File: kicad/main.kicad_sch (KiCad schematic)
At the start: 41 parts, among them J1 Jack-DC, J2 LCD, J3 Addr, J4 IO~{EN}_{[2..7]}, J5 Data, J6 Control, J7 VIA_A, J8 VIA_B, SW1 Step, SW2 Reset, X1 1 MHz

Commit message: Add Traco Power TSR 1-2450
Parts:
- REG1: footprint Package_TO_SOT_THT:TO-220-3_Vertical -> kicad:CONV_TSR_1-2450
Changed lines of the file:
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@@
     (property "Reference" "REG1" (id 0) (at 46.99 109.22 0))
     (property "Value" "TSC 1-2450" (id 1) (at 46.99 111.76 0))
-    (property "Footprint" "Package_TO_SOT_THT:TO-220-3_Vertical" (id 2) (at 46.99 112.395 0)
+    (property "Footprint" "kicad:CONV_TSR_1-2450" (id 2) (at 46.99 112.395 0)
       (effects (font (size 1.27 1.27) italic) hide)
     )
@@
     )
     (path "/997a0ae6-d56b-48b6-8b5e-763a9bca4e41"
-      (reference "REG1") (unit 1) (value "TSC 1-2450") (footprint "Package_TO_SOT_THT:TO-220-3_Vertical")
+      (reference "REG1") (unit 1) (value "TSC 1-2450") (footprint "kicad:CONV_TSR_1-2450")
     )
     (path "/0fe13bfc-8702-4c87-b179-d843f7a65b2c"

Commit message: Update ROM code to be runnable in sim65, increase PCB spacing at borders
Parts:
- RES1, STEP1: footprint Package_TO_SOT_THT:TO-92_Inline -> Package_TO_SOT_THT:TO-92_Inline_Wide
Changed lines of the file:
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@@
       (effects (font (size 1.27 1.27)) (justify right))
     )
-    (property "Footprint" "Package_TO_SOT_THT:TO-92_Inline" (id 2) (at 120.65 100.33 0)
+    (property "Footprint" "Package_TO_SOT_THT:TO-92_Inline_Wide" (id 2) (at 120.65 100.33 0)
       (effects (font (size 1.27 1.27)) hide)
     )
@@
       (effects (font (size 1.27 1.27)) (justify right))
     )
-    (property "Footprint" "Package_TO_SOT_THT:TO-92_Inline" (id 2) (at 95.25 100.33 0)
+    (property "Footprint" "Package_TO_SOT_THT:TO-92_Inline_Wide" (id 2) (at 95.25 100.33 0)
       (effects (font (size 1.27 1.27)) hide)
     )
@@
     )
     (path "/0fe13bfc-8702-4c87-b179-d843f7a65b2c"
-      (reference "RES1") (unit 1) (value "DS1813") (footprint "Package_TO_SOT_THT:TO-92_Inline")
+      (reference "RES1") (unit 1) (value "DS1813") (footprint "Package_TO_SOT_THT:TO-92_Inline_Wide")
     )
     (path "/568d8db0-0878-4f6c-a240-e9c0b9b07dff"
@@
     )
     (path "/5f1426dc-69bd-4410-9694-fac63644cb08"
-      (reference "STEP1") (unit 1) (value "DS1813") (footprint "Package_TO_SOT_THT:TO-92_Inline")
+      (reference "STEP1") (unit 1) (value "DS1813") (footprint "Package_TO_SOT_THT:TO-92_Inline_Wide")
     )
     (path "/cdb98851-649e-4ab7-9299-efd45c6ad697"

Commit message: V11
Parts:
- added C6: 0.1uF, Capacitor_THT:C_Disc_D3.0mm_W2.0mm_P2.50mm, symbol Device:C
- added C8, C9: 20nF, Capacitor_THT:C_Disc_D3.0mm_W2.0mm_P2.50mm, symbol Device:C
- added unit 4 of IO2
- added unit 5 of IO2
- added unit 3 of IO2
- added unit 1 of IO2
- added unit 4 of RW1
- added U1: 8580, Package_DIP:DIP-28_W15.24mm, symbol 65xx:8580
- renumbered C2 to C1, C8 to C10, C7 to C11, C9 to C12, C1 to C2, C6 to C3, C3 to C5, C5 to C7, RW1 to IO2, J7 to J5, J8 to J6, J5 to J7, J6 to J8
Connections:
- net +5V: now also C10.2, C6.1, IO2.14 (VCC); no longer C10.1
- net A_{0}: now also U1.9 (A0)
- net A_{1}: now also U1.10 (A1)
- net A_{2}: now also U1.11 (A2)
- net A_{3}: now also U1.12 (A3)
- net A_{4}: now also U1.13 (A4)
- net D_{0}: now also U1.15 (D0)
- net D_{1}: now also U1.16 (D1)
- net D_{2}: now also U1.17 (D2)
- net D_{3}: now also U1.18 (D3)
- net D_{4}: now also U1.19 (D4)
- net D_{5}: now also U1.20 (D5)
- net D_{6}: now also U1.21 (D6)
- net D_{7}: now also U1.22 (D7)
- net GND: now also C10.1, C6.2, IO2.7 (GND), U1.14 (GND); no longer C10.2
- net R~{W}: now also J2.5 (Pin_5), RW1.10, U1.7 (R/~{W}); no longer RW1.9
- net ~{RES}: now also U1.5 (~{RES})
- net ~{WD}: no longer J2.5 (Pin_5)
- net Ф2: now also CPU1.37 (ϕ0), IO2.5, JP1.2 (C), RW1.9, U1.6 (ϕ2); no longer CPU1.39 (ϕ2), RW1.10
- net LCD~{EN}: no longer names the net of IO1.15 (O0)
- net LCD~{EN}: now also IO2.1, IO2.2; no longer J2.6 (Pin_6)
- new net: C9.1, U1.3 (CAP2A)
- new net: C9.2, U1.4 (CAP2B)
- new net: IO2.3, IO2.4
- new net: IO2.10, IO2.6, IO2.9
- new net: C8.1, U1.1 (CAP1A)
- new net: C8.2, U1.2 (CAP1B)
- new net LCD/EN: IO2.8, J2.6 (Pin_6)
- no-connect marks 11 -> 23
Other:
- note added: "$D400-$D4FF reserved for SID"
- note added: "(PHI1O)"
- note added: "(PHI2)"
- note added: "(PHI2O)"
- note added: "1"
- note added: "2"
- note added: "8 256-byte IO blocks (C000-C7FF)"
- note added: "Memory"
- note added: "Notes:"
- note added: "The Heart"
- note added: "The Mind"
- note added: "The Soul (TBD)"
- note added: "[1] Compatible with: 1008, 2008, & 4008 [2] I initially set this to ~{WD}, but later changed it to R~{W}"
- note removed: "$D400-$CDFF reserved for SID"
- note removed: "8 256-byte I/O segments from C000 to C7FF"
- note removed: "Clock & Reset"
- note removed: "Compatible with 1008, 2008, & 4008"
- title: 6502 SBC -> 65ad02
- moved on the sheet: ADDR1A, ADDR1B, ADDR1C, ADDR1E, C1, C10, C11, C12, C2, C3, C4, C5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

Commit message: V0.12: (PS/2 & 4-bit LCD with VIA), cleanup kicad libs
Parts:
- removed C6: 0.1uF, Capacitor_THT:C_Disc_D3.0mm_W2.0mm_P2.50mm, symbol Device:C
- removed C8, C9: 20nF, Capacitor_THT:C_Disc_D3.0mm_W2.0mm_P2.50mm, symbol Device:C
- removed IO2: 74HC00, Package_DIP:DIP-14_W7.62mm, symbol 74xx:74HC00
- removed J3: Addr, Connector_PinHeader_2.54mm:PinHeader_1x08_P2.54mm_Vertical, symbol Connector:Conn_01x08_Male
- removed J5: VIA_A, Connector_PinHeader_2.54mm:PinHeader_2x07_P2.54mm_Vertical, symbol Connector:Conn_01x14_Male
- removed J6: VIA_B, Connector_PinHeader_2.54mm:PinHeader_2x07_P2.54mm_Vertical, symbol Connector:Conn_01x14_Male
- removed J7: Data, Connector_PinHeader_2.54mm:PinHeader_1x08_P2.54mm_Vertical, symbol Connector:Conn_01x08_Male
- removed J8: Control, Connector_PinHeader_2.54mm:PinHeader_2x05_P2.54mm_Vertical, symbol Connector:Conn_01x10_Male
- removed U1: 8580, Package_DIP:DIP-28_W15.24mm, symbol 65xx:8580
- added J3: Bus, Connector_PinHeader_2.54mm:PinHeader_2x08_P2.54mm_Vertical, symbol Connector:Conn_01x16_Male
- added J4: VIA_B, Connector_PinHeader_2.54mm:PinHeader_2x06_P2.54mm_Vertical, symbol Connector:Conn_01x12_Male
- added J6: Control, Connector_PinHeader_2.54mm:PinHeader_2x04_P2.54mm_Vertical, symbol Connector:Conn_01x08_Male
- added P1: Mini-DIN-6, Custom_Footprints:Connector_Mini-DIN_Female_6Pin_2rows, symbol Custom_Symbols_Library:Mini-DIN_6pins_ver3
- added R8, R9: 1K, Resistor_THT:R_Axial_DIN0204_L3.6mm_D1.6mm_P7.62mm_Horizontal, symbol Device:R
- X1: value 1 MHz -> 4 MHz; footprint Oscillator:Oscillator_DIP-14 -> Package_DIP:DIP-14_W7.62mm_Socket
- renumbered C4 to C3, C5 to C4, C3 to C5, C7 to C6, C11 to C7, C10 to C8, C12 to C9, J4 to J5
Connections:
- net LCD/EN is gone; now on net PA_{4}: J2.6 (Pin_6)
- net +5V: now also J4.2 (Pin_2), J6.2 (Pin_2), P1.4, R8.2, R9.2
- net A_{0}: now also J3.1 (Pin_1); no longer J2.4 (Pin_4)
- net A_{1}: now also J3.2 (Pin_2)
- net A_{2}: now also J3.3 (Pin_3)
- net A_{3}: now also J3.4 (Pin_4)
- net A_{4}: now also J3.5 (Pin_5)
- net A_{5}: now also J3.6 (Pin_6)
- net A_{6}: now also J3.7 (Pin_7)
- net A_{7}: now also J3.8 (Pin_8)
- net D_{0}: now also J3.9 (Pin_9); no longer J2.7 (Pin_7)
- net D_{1}: now also J3.10 (Pin_10); no longer J2.8 (Pin_8)
- net D_{2}: now also J3.11 (Pin_11); no longer J2.9 (Pin_9)
- net D_{3}: now also J3.12 (Pin_12); no longer J2.10 (Pin_10)
- net D_{4}: now also J3.13 (Pin_13); no longer J2.11 (Pin_11)
- net D_{5}: now also J3.14 (Pin_14); no longer J2.12 (Pin_12)
- net D_{6}: now also J3.15 (Pin_15); no longer J2.13 (Pin_13)
- net D_{7}: now also J3.16 (Pin_16); no longer J2.14 (Pin_14)
- net GND: now also J4.1 (Pin_1), J6.1 (Pin_1), P1.3
- net R~{W}: now also J6.3 (Pin_3); no longer J2.5 (Pin_5)
- net VIA~{EN}: now also IO1.15 (O0); no longer IO1.14 (O1)
- net ~{IRQ}: now also J6.7 (Pin_7)
- net ~{RD}: now also J6.4 (Pin_4)
- net ~{RES}: now also J6.8 (Pin_8)
- net ~{WD}: now also J6.5 (Pin_5)
- net Ф2: now also J6.6 (Pin_6)
- net at VIA1.17 (PB7): now also J4.10 (Pin_10)
- net at VIA1.18 (CB1): now also J4.11 (Pin_11)
- net at VIA1.19 (CB2): now also J4.12 (Pin_12)
- net at VIA1.10 (PB0): now also J4.3 (Pin_3)
- net at VIA1.11 (PB1): now also J4.4 (Pin_4)
- net at VIA1.12 (PB2): now also J4.5 (Pin_5)
- net at VIA1.13 (PB3): now also J4.6 (Pin_6)
- net at VIA1.14 (PB4): now also J4.7 (Pin_7)
- net at VIA1.15 (PB5): now also J4.8 (Pin_8)
- net at VIA1.16 (PB6): now also J4.9 (Pin_9)
- net PA_{7}: now reaches VIA1.9 (PA7)
- net PA_{7}: now also P1.1, R9.1
- net CA1: now reaches VIA1.40 (CA1)
- net CA1: now also P1.5, R8.1
- net PA_{0}: now reaches VIA1.2 (PA0)
- net PA_{0}: now also J2.11 (Pin_11)
- net PA_{1}: now reaches VIA1.3 (PA1)
- net PA_{1}: now also J2.12 (Pin_12)
- net PA_{2}: now reaches VIA1.4 (PA2)
- net PA_{2}: now also J2.13 (Pin_13)
- net PA_{3}: now reaches VIA1.5 (PA3)
- net PA_{3}: now also J2.14 (Pin_14)
- net PA_{4}: now reaches VIA1.6 (PA4)
- net PA_{5}: now reaches VIA1.7 (PA5)
- net PA_{5}: now also J2.5 (Pin_5)
- net PA_{6}: now reaches VIA1.8 (PA6)
- net PA_{6}: now also J2.4 (Pin_4)
- no-connect marks 23 -> 22
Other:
- note added: "PS/2 Keyboard Connector"
- note added: "[1] Compatible with: 1008, 2008, & 4008"
- note removed: "$D100-$D1FF"
- note removed: "2"
- note removed: "The Soul (TBD)"
- note removed: "[1] Compatible with: 1008, 2008, & 4008 [2] I initially set this to ~{WD}, but later changed it to R~{W}"
- moved on the sheet: ADDR1A, ADDR1B, ADDR1C, ADDR1D, ADDR1E, C3, C5, C7, IO1, J5, RV1, RW1A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

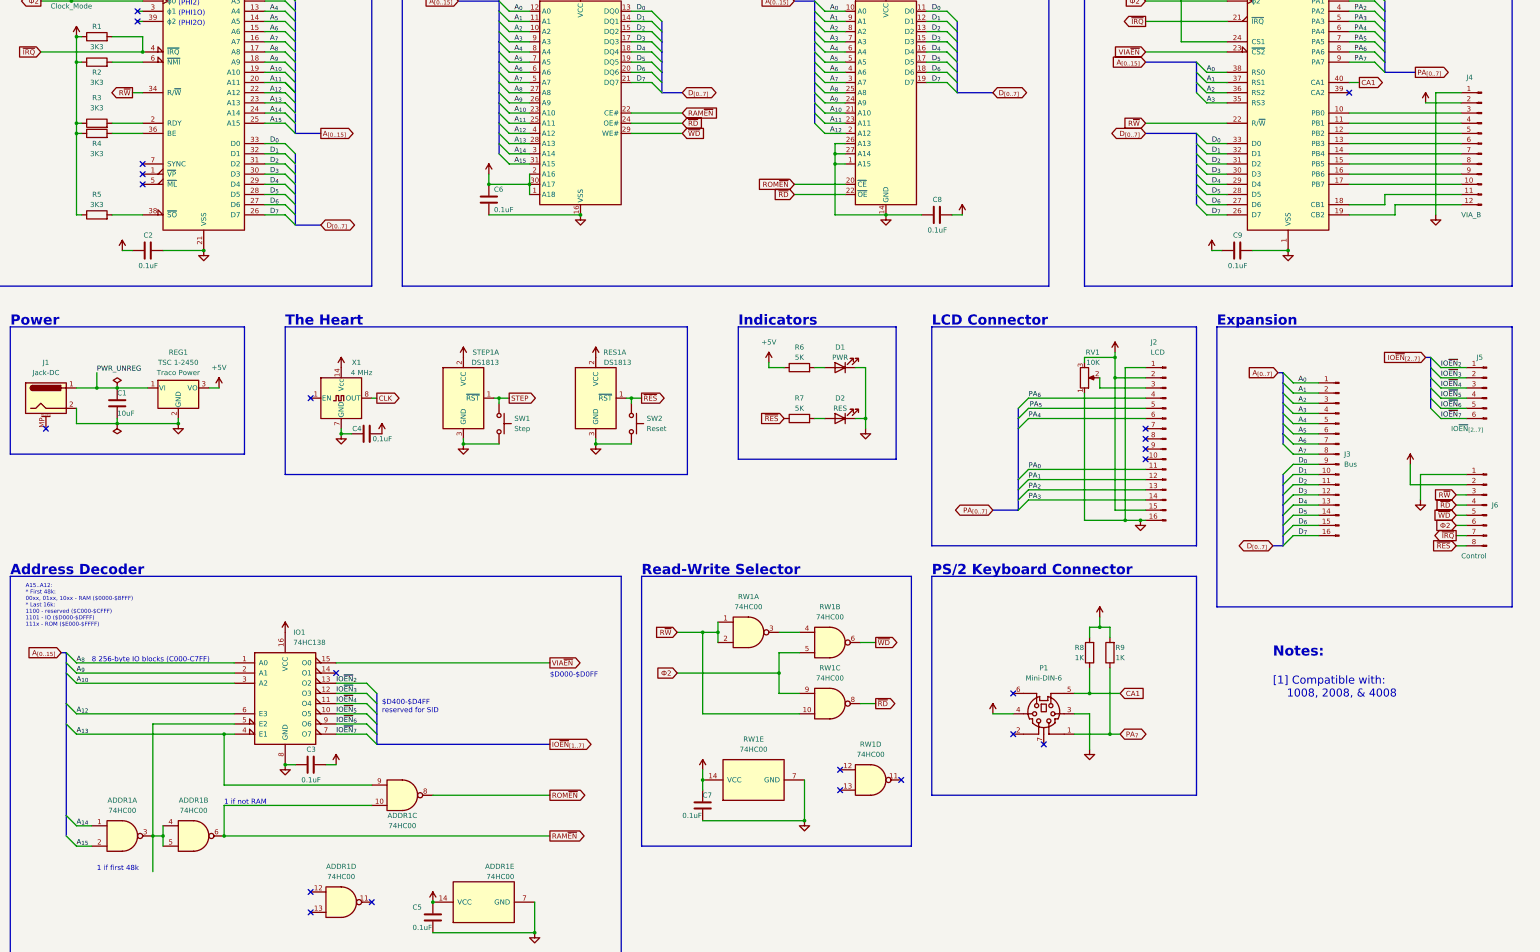
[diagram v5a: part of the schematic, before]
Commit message: Test illegal opcodes, update SPI pin assignments, update V12 PCB
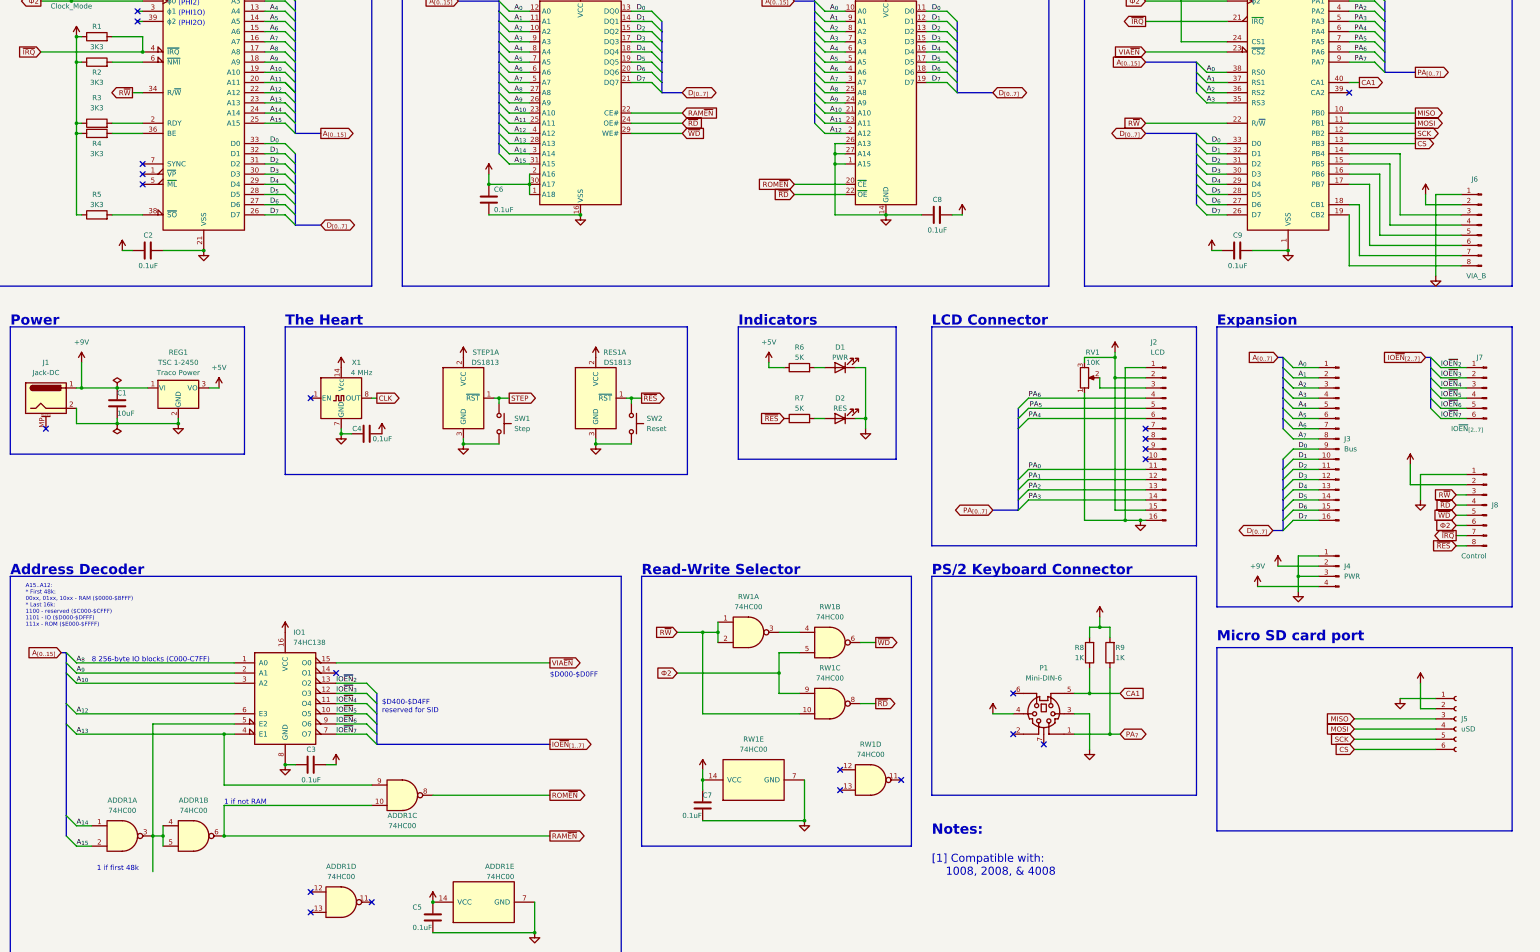
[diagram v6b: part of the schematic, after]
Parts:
- removed J4: VIA_B, Connector_PinHeader_2.54mm:PinHeader_2x06_P2.54mm_Vertical, symbol Connector:Conn_01x12_Male
- added J4: PWR, Connector_PinHeader_2.54mm:PinHeader_2x02_P2.54mm_Vertical, symbol Connector:Conn_01x04_Male
- added J5: uSD, Connector_PinSocket_2.54mm:PinSocket_1x06_P2.54mm_Vertical, symbol Connector:Conn_01x06_Female
- added J6: VIA_B, Connector_PinHeader_2.54mm:PinHeader_2x04_P2.54mm_Vertical, symbol Connector:Conn_01x08_Male
- R1, R2, R3, R4, R5, R8, R9: footprint Resistor_THT:R_Axial_DIN0204_L3.6mm_D1.6mm_P7.62mm_Horizontal -> Resistor_THT:R_Axial_DIN0204_L3.6mm_D1.6mm_P2.54mm_Vertical
- renumbered J5 to J7, J6 to J8
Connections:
- net +5V: now also J4.2 (Pin_2), J5.2 (Pin_2), J6.2 (Pin_2)
- net GND: now also J4.1 (Pin_1), J4.3 (Pin_3), J5.1 (Pin_1), J6.1 (Pin_1)
- net MISO: now reaches VIA1.10 (PB0)
- net MISO: now also J5.3 (Pin_3)
- net MOSI: now reaches VIA1.11 (PB1)
- net MOSI: now also J5.4 (Pin_4)
- net SCK: now reaches VIA1.12 (PB2)
- net SCK: now also J5.5 (Pin_5)
- net CS: now reaches VIA1.13 (PB3)
- net CS: now also J5.6 (Pin_6)
- net at VIA1.14 (PB4): now also J6.3 (Pin_3)
- net at VIA1.15 (PB5): now also J6.4 (Pin_4)
- net at VIA1.16 (PB6): now also J6.5 (Pin_5)
- net at VIA1.17 (PB7): now also J6.6 (Pin_6)
- net at VIA1.18 (CB1): now also J6.7 (Pin_7)
- net at VIA1.19 (CB2): now also J6.8 (Pin_8)
- net PWR_UNREG renamed +9V
- net +9V: now also J4.4 (Pin_4)
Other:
- note added: "Micro SD card port"
- moved on the sheet: J3

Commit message: Refactor ROM code to use carry flag for errors.Add Aries low-profile ZIF socket to V12 board.
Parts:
- REG1: footprint kicad:CONV_TSR_1-2450 -> footprints:CONV_TSR_1-2450
- ROM1: footprint Socket:DIP_Socket-28_W11.9_W12.7_W15.24_W17.78_W18.5_3M_228-1277-00-0602J -> 28-526-10:DIPS1524W61P254L4191H673Q28N

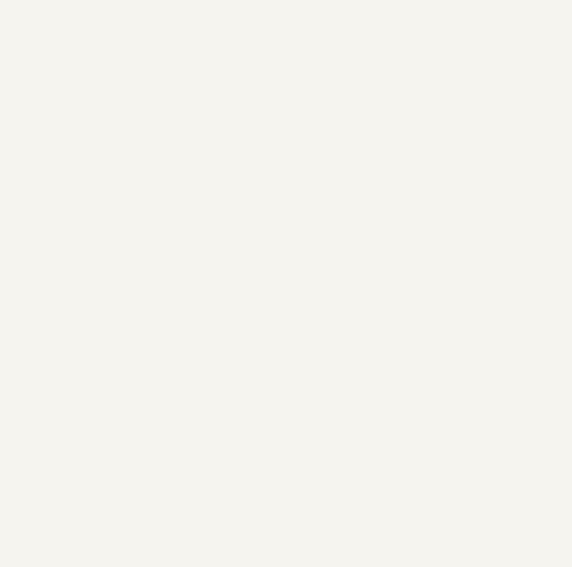
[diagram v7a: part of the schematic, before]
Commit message: Update ATtiny PAL rendering timings
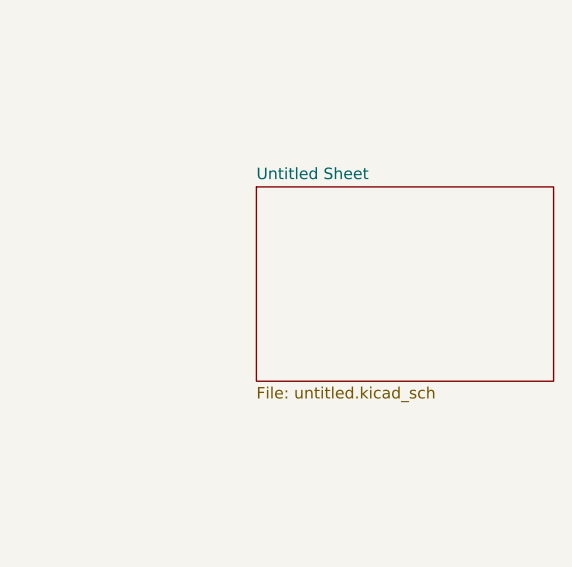
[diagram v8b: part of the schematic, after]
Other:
- added sheet Untitled Sheet (untitled.kicad_sch)
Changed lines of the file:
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@@
+    )
+  )
+  (sheet (at 441.96 102.87) (size 33.02 21.59) (fields_autoplaced)
+    (stroke (width 0.1524) (type solid))
+    (fill (color 0 0 0 0.0000))
+    (property "Sheetname" "Untitled Sheet" (at 441.96 102.1584 0)
+      (effects (font (size 1.27 1.27)) (justify left bottom))
+    )
+    (property "Sheetfile" "untitled.kicad_sch" (at 441.96 125.0446 0)
+      (effects (font (size 1.27 1.27)) (justify left top))
+    )
+    (instances
+      (project "main"
+        (path "/ee3e9410-932c-4ddb-8ce8-606010f57976" (page "2"))
+      )
     )
   )
